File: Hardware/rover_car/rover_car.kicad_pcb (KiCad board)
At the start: 2 copper layers, 40 x 70 mm, 30 parts, among them J1 Conn_01x06_Female, J3 Screw_Terminal_01x02, M1 Motor_DC, M2 Motor_DC, M3 Motor_DC, M4 Motor_DC, M5 Motor_DC, M6 Motor_DC, U1 DRV8833PWP, U2 DRV8833PWP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

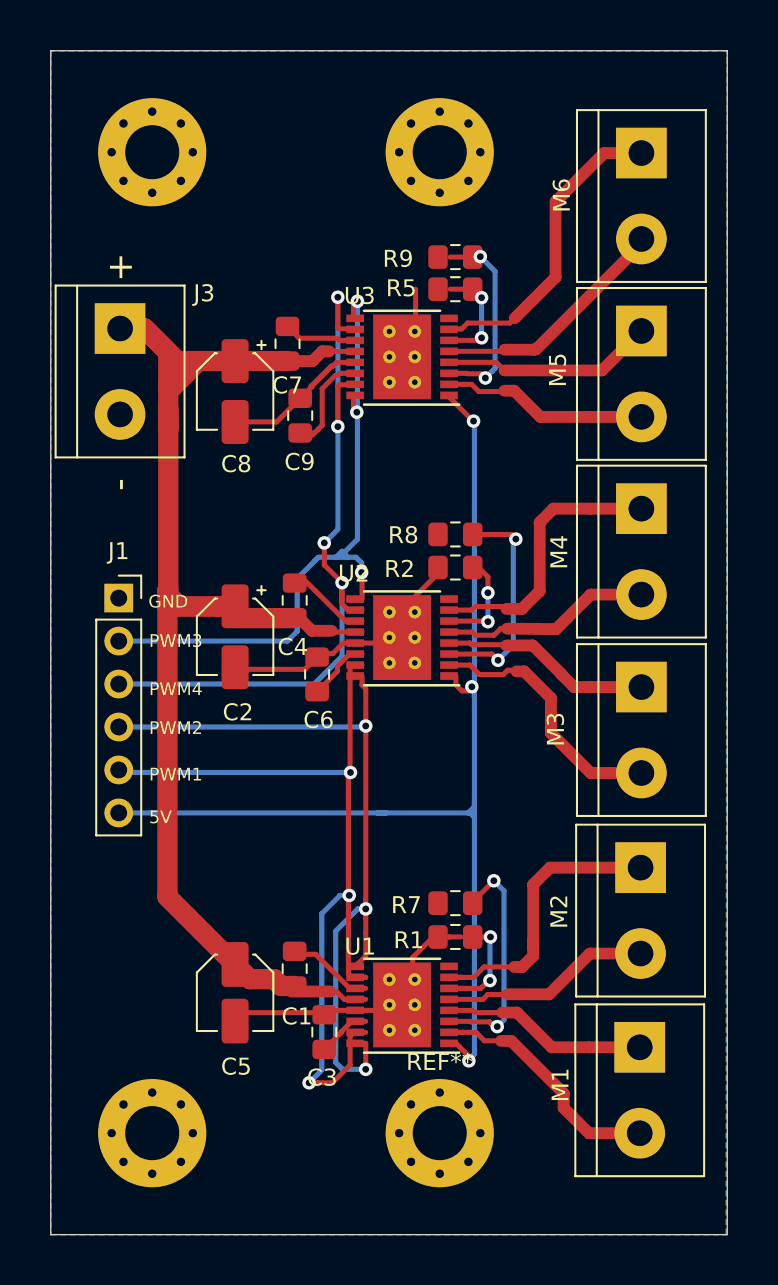
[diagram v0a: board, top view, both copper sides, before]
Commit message: fix corners
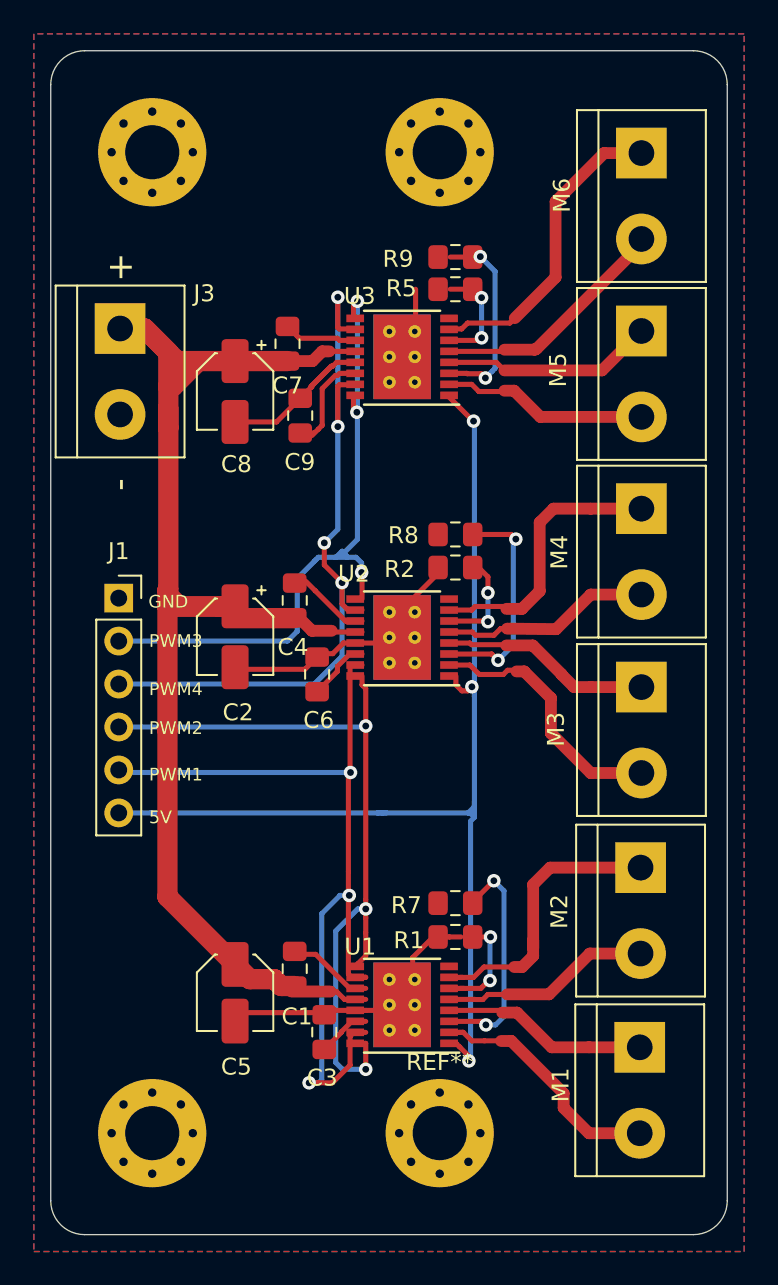
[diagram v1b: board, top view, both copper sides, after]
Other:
- outline, holes or cut-outs redrawn
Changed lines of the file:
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@@
   (general
     (thickness 1.6)
-    (drawings 22)
-    (tracks 420)
+    (drawings 26)
+    (tracks 418)
     (zones 0)
     (modules 30)
@@
     )
   )
+  (gr_arc (start 171 97) (end 171 99) (angle -90) (layer Edge.Cuts) (width 0.05))
+  (gr_arc (start 135 97) (end 133 97) (angle -90) (layer Edge.Cuts) (width 0.05))
+  (gr_arc (start 171 31) (end 173 31) (angle -90) (layer Edge.Cuts) (width 0.05))
+  (gr_arc (start 135 31) (end 135 29) (angle -90) (layer Edge.Cuts) (width 0.05))
   (dimension 70 (width 0.12) (layer B.SilkS)
     (gr_text "70,000 mm" (at 185.27 64 270) (layer B.SilkS)
@@
     (arrow2b (pts (xy 184 29) (xy 184.586421 30.126504)))
   )
-  (gr_line (start 133 99) (end 173 99) (layer Edge.Cuts) (width 0.05))
-  (gr_line (start 133 29) (end 133 99) (layer Edge.Cuts) (width 0.05))
-  (gr_line (start 173 29) (end 133 29) (layer Edge.Cuts) (width 0.05))
-  (gr_line (start 173 99) (end 173 29) (layer Edge.Cuts) (width 0.05))
+  (gr_line (start 135 99) (end 171 99) (layer Edge.Cuts) (width 0.05))
+  (gr_line (start 133 31) (end 133 97) (layer Edge.Cuts) (width 0.05))
+  (gr_line (start 171 29) (end 135 29) (layer Edge.Cuts) (width 0.05))
+  (gr_line (start 173 97) (end 173 31) (layer Edge.Cuts) (width 0.05))
   (dimension 40 (width 0.12) (layer B.SilkS)
     (gr_text "40,000 mm" (at 153 105.27) (layer B.SilkS)
@@
   (segment (start 160.57173 85.87173) (end 162.625 87.925) (width 0.7) (layer F.Cu) (net 12))
   (segment (start 164.825 87.925) (end 167.825 87.925) (width 0.7) (layer F.Cu) (net 12))
-  (segment (start 158.075281 85.87173) (end 159.69673 85.87173) (width 0.3) (layer F.Cu) (net 12))
-  (segment (start 156.55 85.74) (end 157.943551 85.74) (width 0.3) (layer F.Cu) (net 12))
-  (segment (start 157.943551 85.74) (end 158.075281 85.87173) (width 0.3) (layer F.Cu) (net 12))
-  (segment (start 158.145996 87.04) (end 158.645998 87.540002) (width 0.3) (layer F.Cu) (net 13))
-  (segment (start 158.645998 87.540002) (end 159.484998 87.540002) (width 0.3) (layer F.Cu) (net 13))
+  (segment (start 159.565 85.74) (end 159.69673 85.87173) (width 0.3) (layer F.Cu) (net 12))
+  (segment (start 156.55 85.74) (end 159.565 85.74) (width 0.3) (layer F.Cu) (net 12))
   (segment (start 163.325001 91.505001) (end 164.825 93.005) (width 0.7) (layer F.Cu) (net 13))
   (segment (start 163.325001 90.645001) (end 163.325001 91.505001) (width 0.7) (layer F.Cu) (net 13))
@@
   (segment (start 156.55 87.04) (end 157.39 87.04) (width 0.3) (layer F.Cu) (net 13))
   (segment (start 157.175 87.04) (end 157.39 87.04) (width 0.3) (layer F.Cu) (net 13))
-  (segment (start 157.39 87.04) (end 158.145996 87.04) (width 0.3) (layer F.Cu) (net 13))
+  (segment (start 157.890002 87.540002) (end 158.645998 87.540002) (width 0.3) (layer F.Cu) (net 13))
+  (segment (start 158.645998 87.540002) (end 159.484998 87.540002) (width 0.3) (layer F.Cu) (net 13))
+  (segment (start 157.39 87.04) (end 157.890002 87.540002) (width 0.3) (layer F.Cu) (net 13))
   (segment (start 160.4 83.175) (end 160.875 83.175) (width 0.7) (layer F.Cu) (net 14))
   (segment (start 161.525 82.525) (end 161.525 81.6) (width 0.7) (layer F.Cu) (net 14))
@@
   (segment (start 156.955 65.97) (end 156.955 66.495) (width 0.3) (layer F.Cu) (net 27))
   (segment (start 156.955 66.495) (end 157.309307 66.849307) (width 0.3) (layer F.Cu) (net 27))
-  (segment (start 158.05 88.325) (end 157.825 88.55) (width 0.3) (layer B.Cu) (net 27))
   (segment (start 152.315 74.065) (end 152.61 74.065) (width 0.3) (layer B.Cu) (net 27))
   (segment (start 152.61 74.065) (end 152.865 74.065) (width 0.3) (layer B.Cu) (net 27))
@@
   (segment (start 157.659283 66.849307) (end 157.901177 66.607413) (width 0.3) (layer F.Cu) (net 27))
   (via (at 157.901177 66.607413) (size 0.8) (drill 0.4) (layers F.Cu B.Cu) (net 27))
-  (segment (start 158.05 74.325) (end 158.05 79.3) (width 0.3) (layer B.Cu) (net 27))
-  (segment (start 158.05 79.3) (end 158.05 88.325) (width 0.3) (layer B.Cu) (net 27))
   (segment (start 137.02 74.065) (end 138.935 74.065) (width 0.3) (layer B.Cu) (net 27))
   (segment (start 138.935 74.065) (end 152.315 74.065) (width 0.3) (layer B.Cu) (net 27))
@@
   (segment (start 156.55 87.69) (end 156.965 87.69) (width 0.3) (layer F.Cu) (net 27))
   (segment (start 156.965 87.69) (end 157.175 87.9) (width 0.3) (layer F.Cu) (net 27))
-  (via (at 159.4 86.7) (size 0.8) (drill 0.4) (layers F.Cu B.Cu) (net 28))
+  (segment (start 158.05 74.325) (end 157.825 74.55) (width 0.3) (layer B.Cu) (net 27))
+  (segment (start 157.825 74.55) (end 157.825 86.320998) (width 0.3) (layer B.Cu) (net 27))
+  (segment (start 157.825 86.320998) (end 157.825 88.55) (width 0.3) (layer B.Cu) (net 27))
   (via (at 159.2 78.075) (size 0.8) (drill 0.4) (layers F.Cu B.Cu) (net 28))
   (segment (start 157.95 79.325) (end 159.2 78.075) (width 0.3) (layer F.Cu) (net 28))
   (segment (start 157.95 79.4) (end 157.95 79.325) (width 0.3) (layer F.Cu) (net 28))
+  (via (at 158.73 86.6) (size 0.8) (drill 0.4) (layers F.Cu B.Cu) (net 28))
+  (segment (start 158.52 86.39) (end 158.73 86.6) (width 0.3) (layer F.Cu) (net 28))
+  (segment (start 156.55 86.39) (end 158.52 86.39) (width 0.3) (layer F.Cu) (net 28))
   (segment (start 159.8 78.675) (end 159.2 78.075) (width 0.3) (layer B.Cu) (net 28))
-  (segment (start 159.8 86.3) (end 159.8 78.675) (width 0.3) (layer B.Cu) (net 28))
-  (segment (start 159.4 86.7) (end 159.8 86.3) (width 0.3) (layer B.Cu) (net 28))
-  (segment (start 159.225 86.7) (end 159.4 86.7) (width 0.3) (layer F.Cu) (net 28))
-  (segment (start 158.946741 86.421741) (end 159.225 86.7) (width 0.3) (layer F.Cu) (net 28))
-  (segment (start 157.847459 86.421741) (end 158.946741 86.421741) (width 0.3) (layer F.Cu) (net 28))
-  (segment (start 156.55 86.39) (end 157.815718 86.39) (width 0.3) (layer F.Cu) (net 28))
-  (segment (start 157.815718 86.39) (end 157.847459 86.421741) (width 0.3) (layer F.Cu) (net 28))
+  (segment (start 159.8 86.095685) (end 159.8 78.675) (width 0.3) (layer B.Cu) (net 28))
+  (segment (start 159.295685 86.6) (end 159.8 86.095685) (width 0.3) (layer B.Cu) (net 28))
+  (segment (start 158.73 86.6) (end 159.295685 86.6) (width 0.3) (layer B.Cu) (net 28))
   (via (at 159.446739 65.041077) (size 0.8) (drill 0.4) (layers F.Cu B.Cu) (net 29))
   (segment (start 156.955 64.67) (end 159.075662 64.67) (width 0.3) (layer F.Cu) (net 29))
@@
   (segment (start 150.084315 78.965685) (end 150.084315 78.94299) (width 0.3) (layer B.Cu) (net 34))
   (segment (start 149.025 80.025) (end 150.084315 78.965685) (width 0.3) (layer B.Cu) (net 34))
-  (segment (start 148.275 90.025) (end 149.025 89.275) (width 0.3) (layer B.Cu) (net 34))
-  (segment (start 149.025 89.275) (end 149.025 80.025) (width 0.3) (layer B.Cu) (net 34))
+  (segment (start 149.025 89.840685) (end 149.025 80.025) (width 0.3) (layer B.Cu) (net 34))
+  (segment (start 148.840685 90.025) (end 149.025 89.840685) (width 0.3) (layer B.Cu) (net 34))
+  (segment (start 148.275 90.025) (end 148.840685 90.025) (width 0.3) (layer B.Cu) (net 34))
   (zone (net 3) (net_name GND) (layer B.Cu) (hatch edge 0.508)
     (connect_pads (clearance 0.508))
@@
     (polygon
       (pts
-        (xy 173 29) (xy 133 29) (xy 133 99) (xy 172.929485 99)
+        (xy 174 28) (xy 132 28) (xy 132 100) (xy 174 100)
       )
     )
@@
     (polygon
       (pts
-        (xy 173 29) (xy 133 29) (xy 133 99) (xy 173 99)
+        (xy 174 28) (xy 132 28) (xy 132 100) (xy 174 100)
       )
     )

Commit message: Fix component number and etching
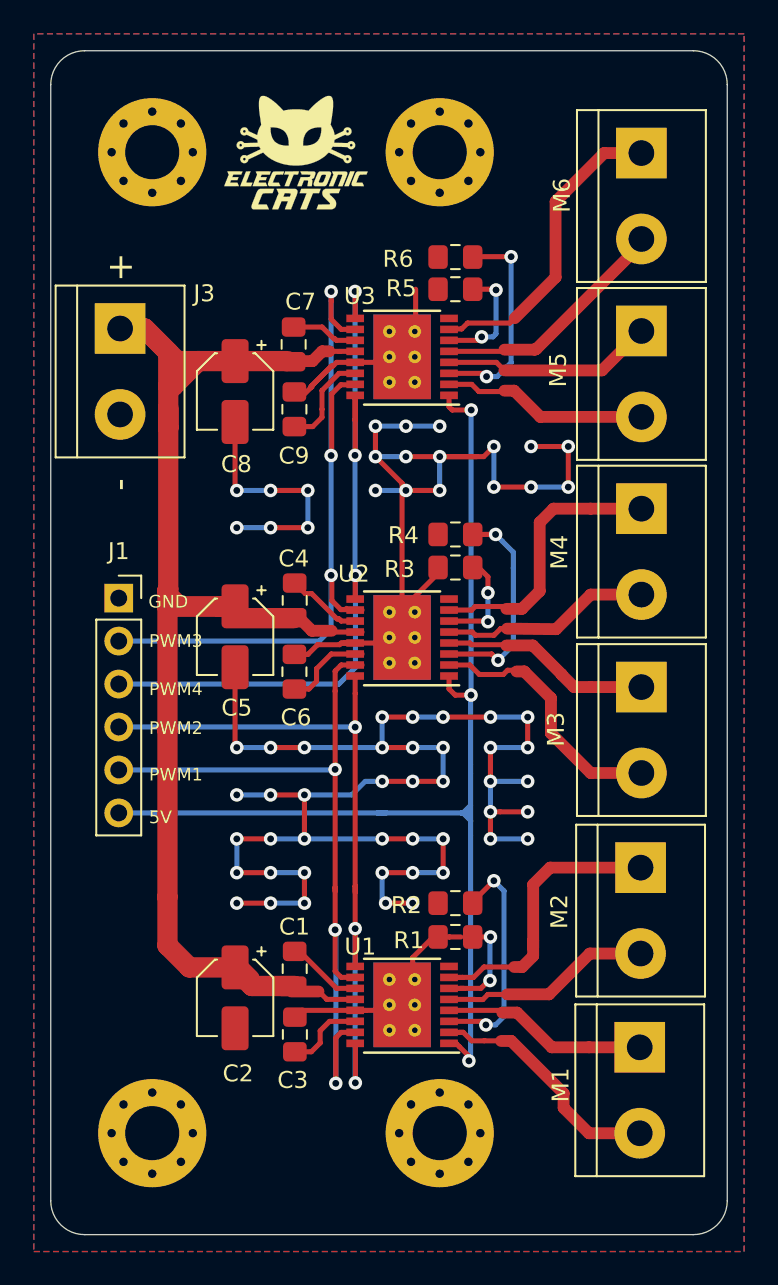
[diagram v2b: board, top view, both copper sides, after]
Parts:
- added G***: LOGO, Aesthetics:electronic_cats_logo_8x6, F.Cu at (147.5, 35.0)
- C5: footprint Capacitor_SMD:C_Elec_4x5.4 -> Capacitor_SMD:CP_Elec_4x5.4
- moved C2 21.4 mm to (143.9, 85.0)
- moved C5 21.1 mm to (143.9, 63.6)
- moved C3 1.74 mm to (147.4, 87.2)
- moved C6 1.35 mm to (147.4, 65.7)
- moved C9 0.51 mm to (147.4, 50.2)
- moved C7 0.36 mm to (147.4, 46.4)
- renumbered R7 to R2, R2 to R3, R8 to R4, R9 to R6
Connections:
- J1 pad 2: /GPIO14 -> /GPIO15
- J1 pad 3: /GPIO15 -> /GPIO14
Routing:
- net GND: track 53.6 -> 197.6 mm, vias 0 -> 63
- net /GPIO14: track 39.3 -> 44.7 mm
- net /GPIO12: track 52.2 -> 47.1 mm
- net +12V: track 99.3 -> 102.4 mm
- net /GPIO4: track 46.0 -> 43.0 mm
- net Net-(C6-Pad1): track 3.75 -> 5.61 mm
- net Net-(C3-Pad1): track 3.49 -> 4.73 mm
- net /GPIO15: track 44.8 -> 45.5 mm, vias 4 -> 3
- net Net-(R6-Pad1): track 11.9 -> 12.6 mm
- net Net-(R4-Pad1): track 13.0 -> 13.7 mm
- net Net-(C1-Pad2): track 5.51 -> 4.88 mm
- net VCC: track 66.5 -> 67.0 mm

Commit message: Update PCB version 1.0
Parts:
- added G***: LOGO, Aesthetics:inventors171x91, F.Cu at (135.8, 82.5)
- moved J1 2.22 mm to (134.8, 61.4)
- moved G*** 0.11 mm to (147.6, 35.0), turned to 270 degrees
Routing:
- net GND: track 197.6 -> 183.9 mm, vias 63 -> 61
- net /GPIO15: track 45.5 -> 51.9 mm
- net /GPIO4: track 43.0 -> 48.8 mm
- net /GPIO14: track 44.7 -> 50.1 mm
- net /GPIO12: track 47.1 -> 50.6 mm
- net VCC: track 67.0 -> 69.2 mm
- net Net-(R2-Pad1): track 13.7 -> 12.1 mm
- net Net-(R3-Pad1): track 5.23 -> 6.60 mm
- net Net-(C4-Pad2): track 4.50 -> 5.34 mm
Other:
- board text added: "12v"
- board text added: "A"
- board text added: "B"
- board text added: "Engine 1"
- board text added: "Engine 2"
- board text added: "Rover Motor Driver v1.0"
- board text added: "Rover Motor Driver v1.0 Vm = 12v Vcc = 5v 1 A / Motor"
